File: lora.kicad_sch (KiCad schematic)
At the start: 26 parts, among them J5 Conn_Coaxial, U3 E22P-915M30S

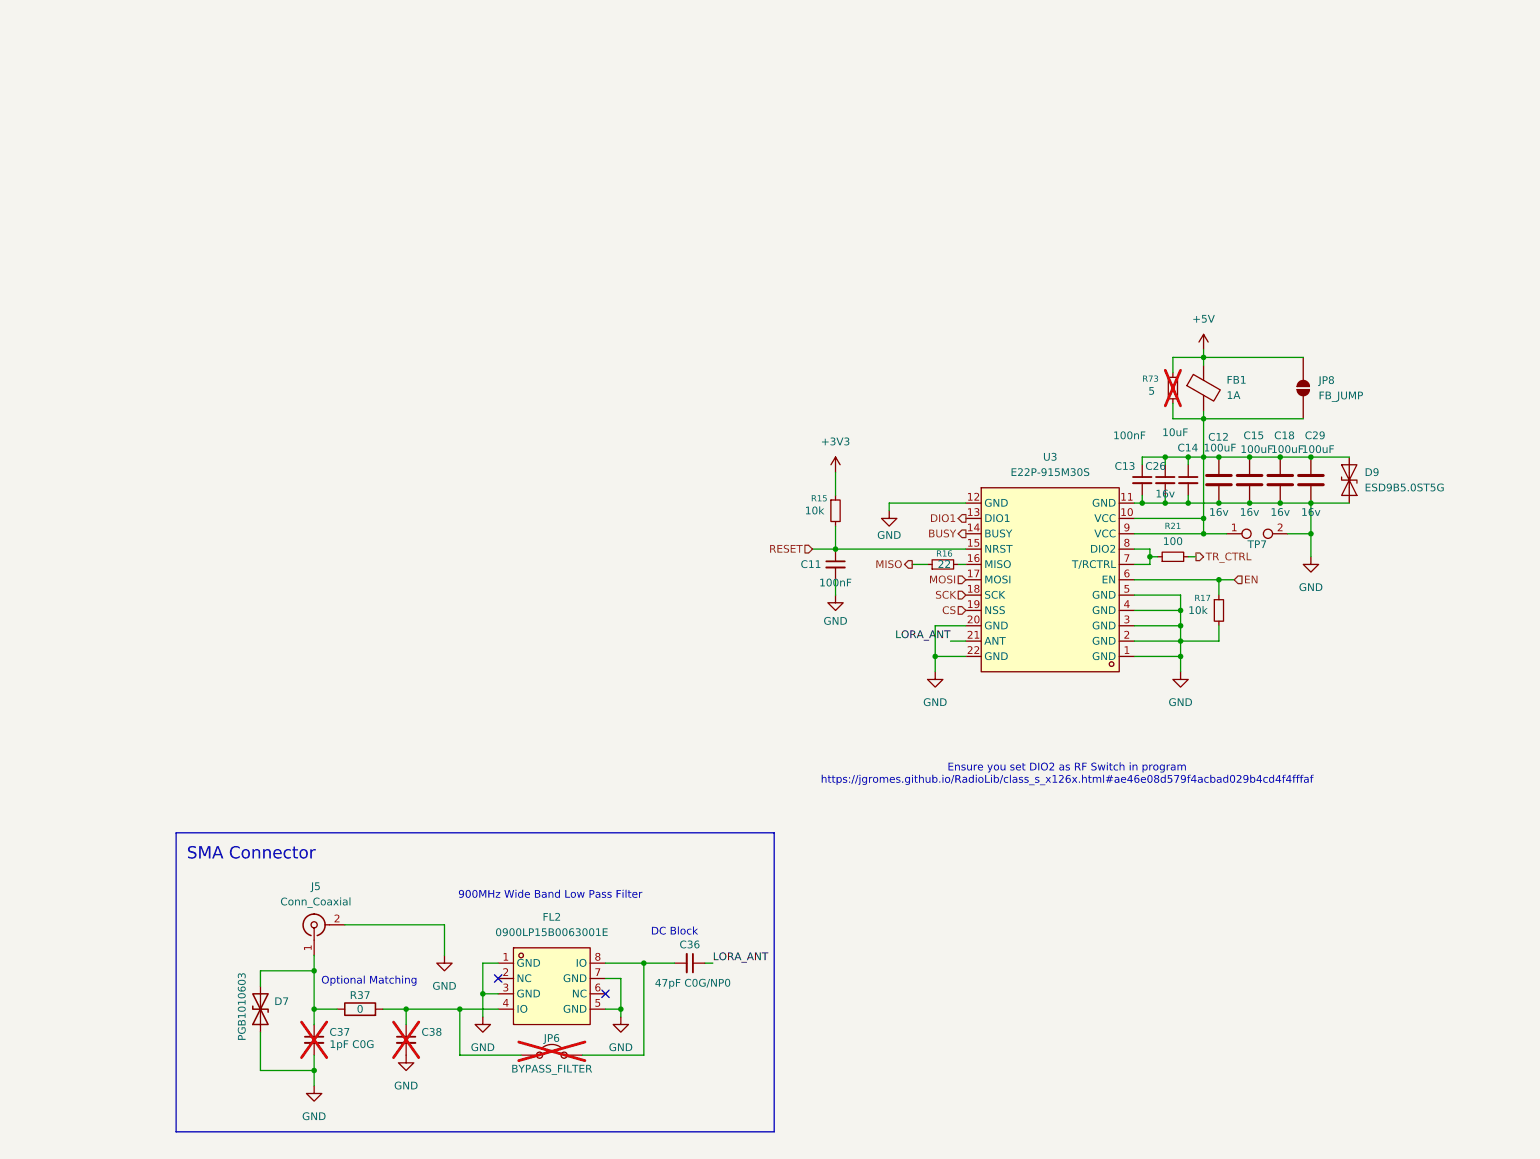
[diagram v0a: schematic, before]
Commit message: rename sheets, add lora antenna detect, seperate charger and regulator schematics, add eFuse to 5v output
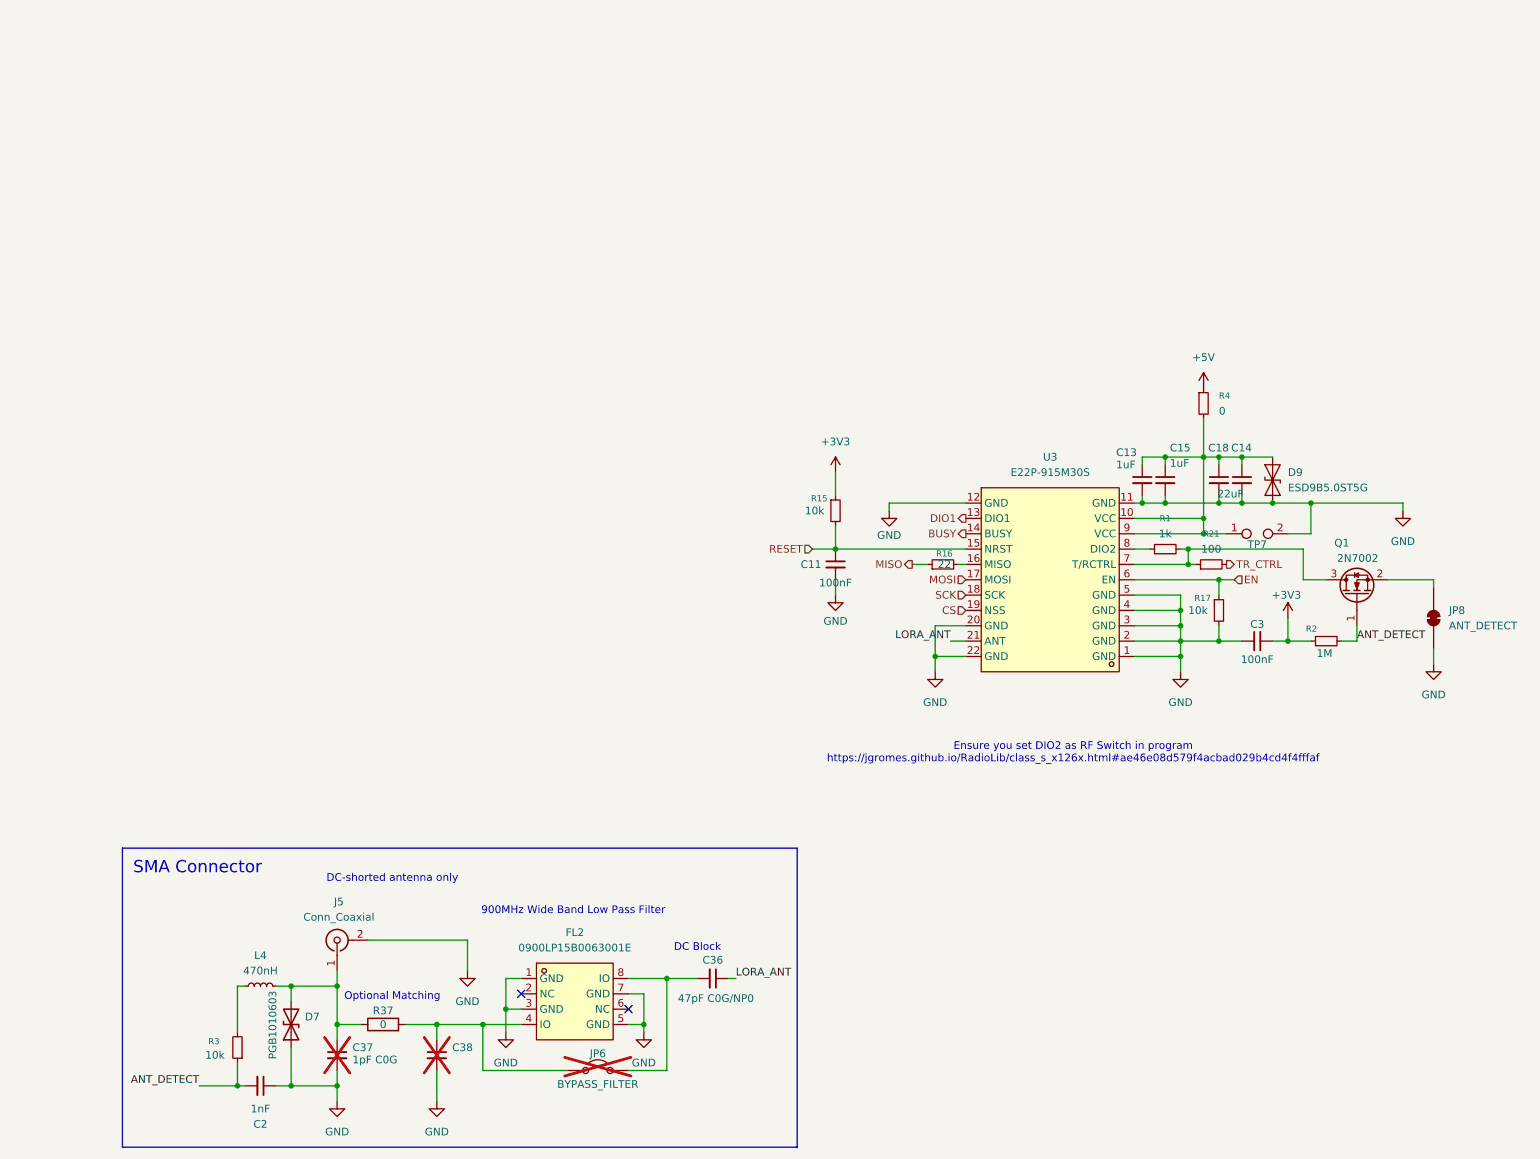
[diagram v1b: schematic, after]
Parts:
- removed C12, C15, C18, C29: 100uF, Capacitor_SMD:C_1210_3225Metric, symbol Device:C
- removed C26: 10uF, Capacitor_SMD:C_0402_1005Metric, symbol Device:C_Small
- removed FB1: 1A, symbol Device:FerriteBead
- removed JP8: FB_JUMP, Jumper:SolderJumper-2_P1.3mm_Open_RoundedPad1.0x1.5mm, symbol Jumper:SolderJumper_2_Open
- removed R73: 5, Capacitor_SMD:C_0603_1608Metric_Pad1.08x0.95mm_HandSolder, symbol Device:R_Small
- added C15: 1uF, Capacitor_SMD:C_0402_1005Metric, symbol Device:C_Small
- added C18: 22uF, Capacitor_SMD:C_0805_2012Metric, symbol Device:C_Small
- added C2: 1nF, symbol Device:C_Small
- added C3: 100nF, symbol Device:C_Small
- added JP8: ANT_DETECT, Jumper:SolderJumper-2_P1.3mm_Bridged_RoundedPad1.0x1.5mm, symbol Jumper:SolderJumper_2_Bridged
- added L4: 470nH, symbol Device:L_Small
- added Q1: 2N7002, Package_TO_SOT_SMD:SOT-23, symbol Transistor_FET:2N7002
- added R1: 1k, symbol Device:R_Small
- added R2: 1M, symbol Device:R_Small
- added R3: 10k, symbol Device:R_Small
- added R4: 0, Resistor_SMD:R_0805_2012Metric, symbol Device:R_Small
- C13: value 100nF -> 1uF; Voltage Rating 16v -> 50V
- C14: value 47uF -> 22uF; Voltage Rating 10V -> 25V
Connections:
- net +3V3: now also C3.2, R2.1
- net +5V: now also R4.1
- net GND: now also C15.2, C18.2, C2.1, C3.1, JP8.1 (A)
- net at C13.1, C14.1, D9.2 (A2)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: now also C15.1, C18.1, R4.2
- net at R21.1, U3.7 (T/RCTRL): now also Q1.3 (D), R1.2; no longer U3.8 (DIO2)
- net at C37.1, D7.2 (A2), J5.1 (In)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: now also L4.2
- new net: R1.1, U3.8 (DIO2)
- new net: L4.1, R3.2
- new net: JP8.2 (B), Q1.2 (S)
- new net ANT_DETECT: C2.2, Q1.1 (G), R2.2, R3.1
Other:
- note added: "DC-shorted antenna only"
- moved on the sheet: C14, C36, C37, C38, D7, D9, FL2, J5, JP6, R21, R37

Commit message: Reworking power rails, adding antenna detection, and organization
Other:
- note added: "DC-shorted antenna only unless JP8 is cut"
- note removed: "DC-shorted antenna only"
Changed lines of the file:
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@@
 		)
 	)
-	(text "DC-shorted antenna only"
+	(text "DC-shorted antenna only unless JP8 is cut"
 		(exclude_from_sim no)
-		(at 61.214 143.51 0)
+		(at 61.214 144.526 0)
 		(effects
 			(font
@@
 		(in_pos_files yes)
 		(dnp no)
-		(fields_autoplaced yes)
 		(property "Reference" "R1"
-			(at 189.23 83.82 90)
+			(at 189.23 86.614 90)
 			(show_name no)
 			(do_not_autoplace no)
@@
 		)
 		(property "Value" "1k"
-			(at 189.23 86.36 90)
+			(at 189.23 88.9 90)
 			(show_name no)
 			(do_not_autoplace no)
@@
 		(in_pos_files yes)
 		(dnp no)
-		(fields_autoplaced yes)
 		(property "Reference" "R21"
-			(at 196.85 86.36 90)
+			(at 196.85 88.138 90)
 			(show_name no)
 			(do_not_autoplace no)
@@
 		)
 		(property "Value" "100"
-			(at 196.85 88.9 90)
-			(show_name no)
-			(do_not_autoplace no)
+			(at 196.85 91.44 90)
+			(show_name no)
+			(do_not_autoplace no)

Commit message: usb-org
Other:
- moved on the sheet: C2, C36, C37, C38, D7, FL2, J5, JP6, L4, R3, R37

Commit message: push to work on laptop2
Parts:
- D9: value ESD9B5.0ST5G -> TPD1E10B06; footprint Diode_SMD:D_SOD-923 -> Package_SON:Texas_DPY0002A_0.6x1mm_P0.65mm; LCSC Part (none) -> C48260
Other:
- company: (none) -> Ryan Di Lorenzo
- title: (none) -> LoRa Module / LoRa Antenna
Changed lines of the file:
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@@
 	(paper "A4")
 	(title_block
+		(title "LoRa Module / LoRa Antenna")
 		(date "2026-05-14")
+		(company "Ryan Di Lorenzo")
 	)
 	(rectangle
@@
 	(wire
 		(pts
+			(xy 200.66 91.44) (xy 199.39 91.44)
+		)
+		(stroke
+			(width 0)
+			(type default)
+		)
+	)
+	(wire
+		(pts
 			(xy 58.42 158.75) (xy 58.42 156.21)
 		)
@@
 		)
 	)
-	(hierarchical_label "EN"
+	(global_label "MISO"
 		(shape input)
+		(at 7.121 1.3498 180)
+		(fields_autoplaced yes)
+		(effects
+			(font
+				(size 1.27 1.27)
+			)
+			(justify right)
+		)
+		(property "Intersheetrefs" "${INTERSHEET_REFS}"
+			(at -0.4604 1.3498 0)
+			(hide yes)
+			(show_name no)
+			(do_not_autoplace no)
+			(effects
+				(font
+					(size 1.27 1.27)
+				)
+				(justify right)
+			)
+		)
+	)
+	(hierarchical_label "EN"
+		(shape passive)
 		(at 200.66 93.98 0)
 		(effects
@@
 	)
 	(hierarchical_label "TR_CTRL"
-		(shape output)
-		(at 199.39 91.44 0)
+		(shape passive)
+		(at 200.66 91.44 0)
 		(effects
 			(font
@@
 			)
 		)
-		(property "Value" "ESD9B5.0ST5G"
+		(property "Value" "TPD1E10B06"
 			(at 209.55 78.7399 90)
 			(show_name no)
@@
 			)
 		)
-		(property "Footprint" "Diode_SMD:D_SOD-923"
+		(property "Footprint" "Package_SON:Texas_DPY0002A_0.6x1mm_P0.65mm"
 			(at 207.01 77.47 0)
 			(hide yes)
@@
 			)
 		)
-		(property "Datasheet" "https://www.onsemi.com/pub/Collateral/ESD9B-D.PDF"
+		(property "Datasheet" ""
 			(at 207.01 77.47 0)
 			(hide yes)
@@
 			)
 		)
-		(property "Description" "ESD protection diode, 5.0Vrwm, SOD-923"
+		(property "Description" ""
+			(at 207.01 77.47 0)
+			(hide yes)
+			(show_name no)
+			(do_not_autoplace no)
+			(effects
+				(font
+					(size 1.27 1.27)
+				)
+			)
+		)
+		(property "LCSC Part" "C48260"
+			(at 207.01 77.47 0)
+			(hide yes)
+			(show_name no)
+			(do_not_autoplace no)
+			(effects
+				(font
+					(size 1.27 1.27)
+				)
+			)
+		)
+		(property "Voltage Rating" ""
+			(at 207.01 77.47 0)
+			(hide yes)
+			(show_name no)
+			(do_not_autoplace no)
+			(effects
+				(font
+					(size 1.27 1.27)
+				)
+			)
+		)
+		(property "Tolerance" ""
+			(at 207.01 77.47 0)
+			(hide yes)
+			(show_name no)
+			(do_not_autoplace no)
+			(effects
+				(font
+					(size 1.27 1.27)
+				)
+			)
+		)
+		(property "Capacitor Rating" ""
 			(at 207.01 77.47 0)
 			(hide yes)
@@
 			(at 170.18 93.98 0)
 			(hide yes)
+			(show_name no)
+			(do_not_autoplace no)
+			(effects
+				(font
+					(size 1.27 1.27)
+				)
+			)
+		)
+		(property "Capacitor Rating" ""
+			(at 170.18 93.98 0)
+			(hide yes)

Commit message: push for review, minor changes
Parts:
- added R74: 0, Resistor_SMD:R_0402_1005Metric, symbol Device:R_Small
- added R75: 10k, Resistor_SMD:R_0402_1005Metric, symbol Device:R_Small
- renumbered C38 to C100, C36 to C101, C11 to C102, C13 to C103, C15 to C104, C18 to C105, C14 to C106, C3 to C107, C2 to C98, C37 to C99, D7 to D14, D9 to D15, J5 to J9, JP6 to JP13, JP8 to JP14, L4 to L3, Q1 to Q10, R3 to R73, R37 to R76, R15 to R77, R16 to R78, R1 to R79, R4 to R80, R21 to R81, R17 to R82, R2 to R83, TP7 to TP6, U3 to U11
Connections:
- net +3V3: now also R74.1
- net EN: now also R75.2
- new net: R74.2, R75.1
